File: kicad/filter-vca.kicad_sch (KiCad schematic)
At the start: 55 parts, among them J37 Conn_01x03_Male, U10 TL074, U12 LM13700, U13 LM13700, U15 TL072

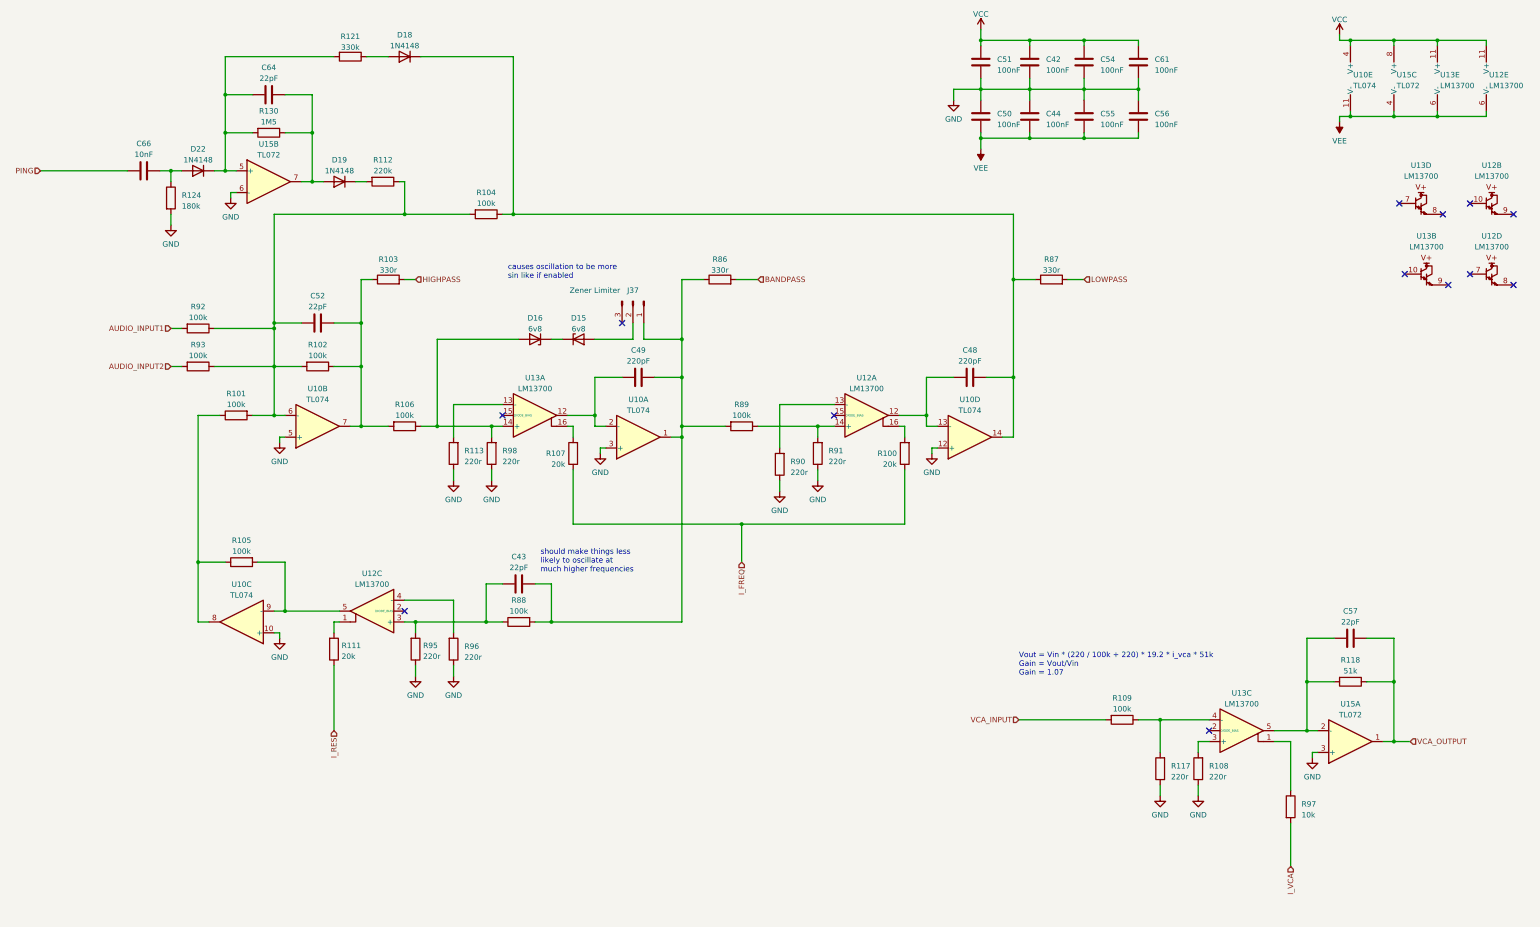
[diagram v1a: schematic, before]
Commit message: Updating board for new footprint libraries
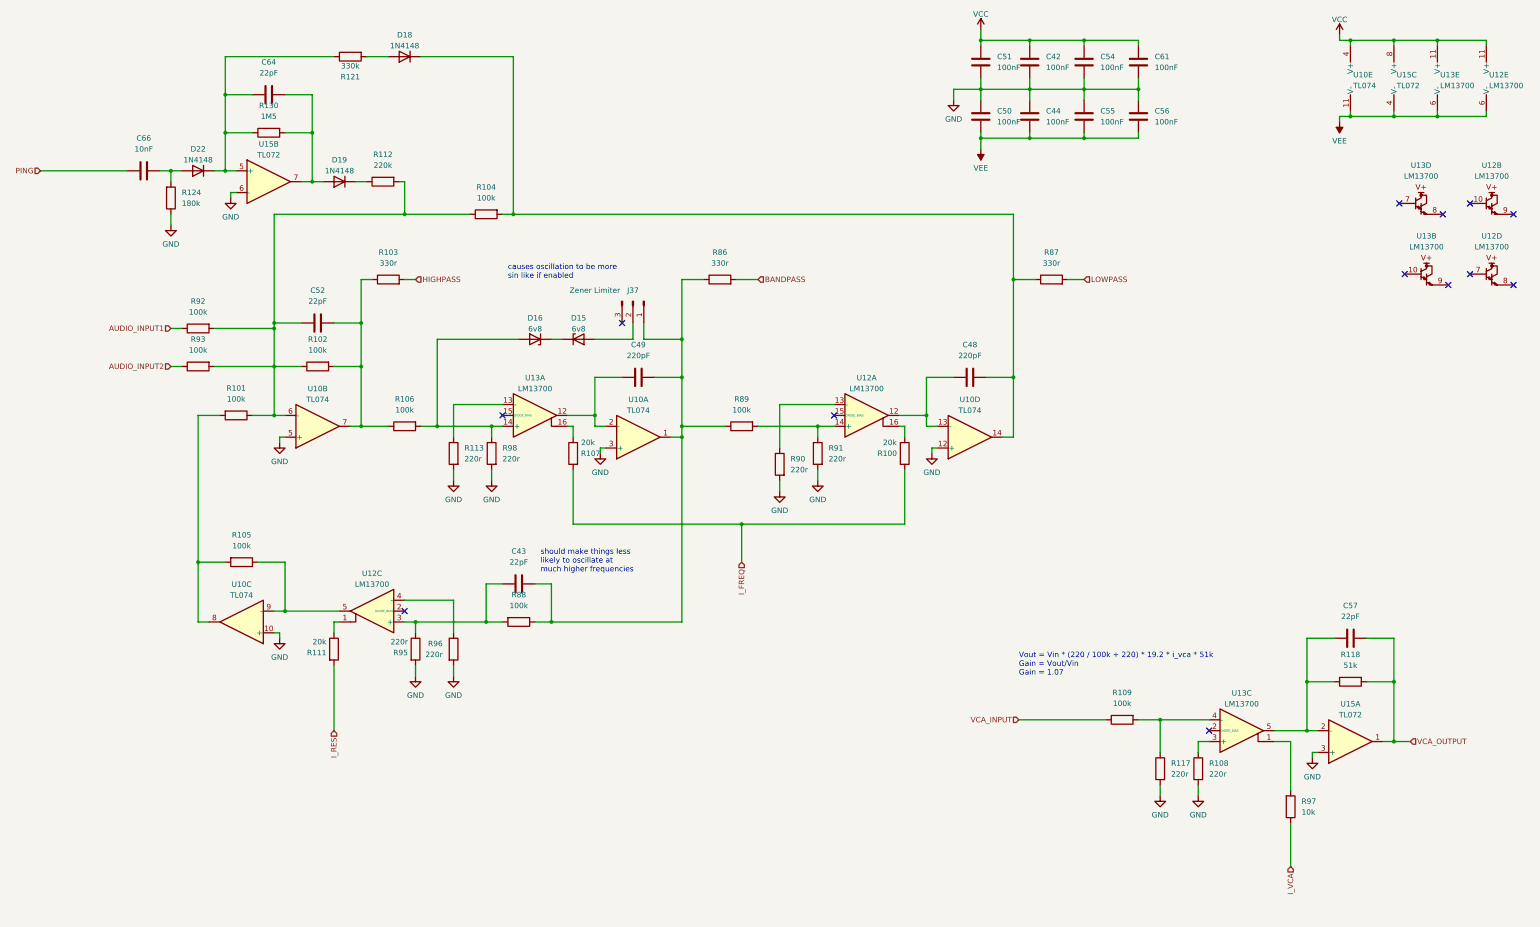
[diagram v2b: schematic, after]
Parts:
- C42, C43, C44, C48, C49, C50, C51, C52, C54, C55, C56, C57, C61, C64, C66: symbol Rumblesan Standard Parts:C -> Rumblesan_Standard_Parts:C
- R100, R101, R102, R104, R105, R106, R107, R108, R109, R111, R112, R113, R117, R118, R121, R124, R130, R88, R89, R90, R91, R92, R93, R95, R96, R97, R98: symbol Rumblesan Standard Parts:R -> Rumblesan_Standard_Parts:R
- U10: footprint Rumblesan_Standard_Parts:DIP-14_W7.62mm_Socket -> Package_DIP:DIP-14_W7.62mm_Socket
- U12, U13: footprint Rumblesan_Standard_Parts:DIP-16_W7.62mm_Socket -> Package_DIP:DIP-16_W7.62mm_Socket
- U15: footprint Rumblesan_Standard_Parts:DIP-8_W7.62mm_Socket -> Package_DIP:DIP-8_W7.62mm_Socket
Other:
- moved on the sheet: R101, R102, R104, R105, R106, R107, R108, R109, R112, R113, R117, R118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

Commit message: Updating with rev03 changes
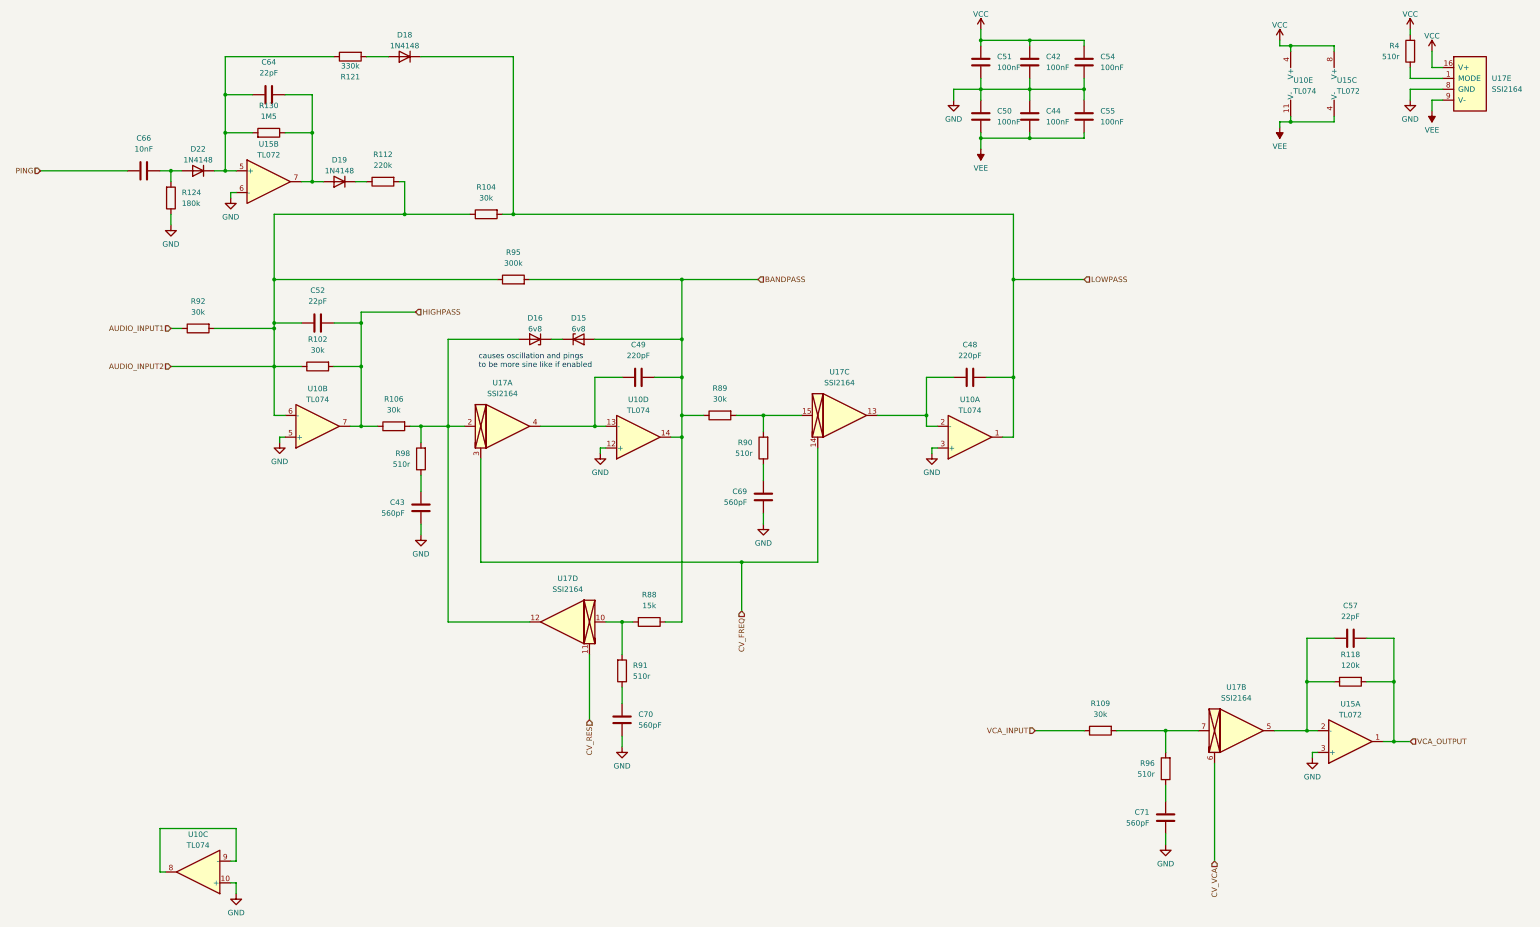
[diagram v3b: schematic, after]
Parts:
- removed C56, C61: 100nF, Rumblesan_Standard_Parts:C_Rect_L7.0mm_W2.5mm_P5.00mm, symbol Rumblesan_Standard_Parts:C
- removed J37: Conn_01x03_Male, Connector_PinHeader_2.54mm:PinHeader_1x03_P2.54mm_Vertical, symbol Connector:Conn_01x03_Pin
- removed R100, R107, R111: 20k, Rumblesan_Standard_Parts:R_Axial_DIN0207_L6.3mm_D2.5mm_P10.16mm_Horizontal, symbol Rumblesan_Standard_Parts:R
- removed R101, R105, R93: 100k, Rumblesan_Standard_Parts:R_Axial_DIN0207_L6.3mm_D2.5mm_P10.16mm_Horizontal, symbol Rumblesan_Standard_Parts:R
- removed R103, R86, R87: 330r, Rumblesan_Standard_Parts:R_Axial_DIN0207_L6.3mm_D2.5mm_P10.16mm_Horizontal, symbol Device:R
- removed R108, R113, R117, R95: 220r, Rumblesan_Standard_Parts:R_Axial_DIN0207_L6.3mm_D2.5mm_P10.16mm_Horizontal, symbol Rumblesan_Standard_Parts:R
- removed R97: 10k, Rumblesan_Standard_Parts:R_Axial_DIN0207_L6.3mm_D2.5mm_P10.16mm_Horizontal, symbol Rumblesan_Standard_Parts:R
- removed U12, U13: LM13700, Package_DIP:DIP-16_W7.62mm_Socket, symbol Amplifier_Operational:LM13700
- added C69, C70, C71: 560pF, Rumblesan_Standard_Parts:C_Rect_L7.0mm_W2.5mm_P5.00mm, symbol Rumblesan_Standard_Parts:C
- added R4: 510r, Rumblesan_Standard_Parts:R_Axial_DIN0207_L6.3mm_D2.5mm_P10.16mm_Horizontal, symbol Rumblesan_Standard_Parts:R
- added R95: 300k, Rumblesan_Standard_Parts:R_Axial_DIN0207_L6.3mm_D2.5mm_P10.16mm_Horizontal, symbol Device:R
- added U17: SSI2164, Package_DIP:DIP-16_W7.62mm_Socket, symbol Rumblesan_Audio_Chips:SSI2164
- C43: value 22pF -> 560pF
- C48, C49: footprint Rumblesan_Standard_Parts:C_Rect_L7.0mm_W2.5mm_P5.00mm -> Capacitor_THT:C_Rect_L7.0mm_W4.5mm_P5.00mm
- R102, R104, R106, R109, R89, R92: value 100k -> 30k
- R118: value 51k -> 120k
- R88: value 100k -> 15k
- R90, R91, R96, R98: value 220r -> 510r
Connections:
- net AUDIO_INPUT2: now also C52.1, R102.2, R104.2, R112.1, R92.1, U10.6 (-), R95.1
- net BANDPASS: now also C49.2, D15.2 (A), R88.2, R89.2, U10.14, R95.2
- net GND: now also C43.2, C44.2, C50.2, C69.2, C70.2, C71.2, U17.8 (GND); no longer C44.1, C50.1, R90.1, R91.1, R96.1, R98.1
- net HIGHPASS: now also C52.2, R102.1, R106.2, U10.7
- net LOWPASS: now also C48.2, D18.1 (K), R104.1, U10.1
- net VCC: now also R4.1, U17.16 (V+)
- net VEE: now also C44.1, C50.1, U17.9 (V-); no longer C44.2, C50.2
- net at C57.1, R118.2, U15.2 (-): now also U17.5
- net at U10.8: now also U10.9 (-)
- net at D16.2 (A), R106.1: now also R98.1, U17.12, U17.2; no longer R98.2
- net at C49.1: now also U10.13 (-), U17.4; no longer U10.2 (-)
- net at C64.1, D22.1 (K), R121.2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: now also R130.1; no longer R130.2
- net at R109.1: now also R96.1, U17.7
- net at C43.1: now also R98.2; no longer R88.1
- net at C64.2, D19.2 (A), U15.7: now also R130.2; no longer R130.1
- net at C48.1: now also U10.2 (-), U17.13; no longer U10.13 (-)
- net at R91.2: now also C70.1; no longer R89.1
- net at R90.2: now also C69.1
- net at R96.2: now also C71.1
- new net: R88.1, R91.1, U17.10
- new net: R4.2, U17.1 (MODE)
- new net: R89.1, R90.1, U17.15
- new net CV_FREQ: U17.14, U17.3
- new net CV_RES: U17.11
- new net CV_VCA: U17.6
- no-connect marks 13 -> 0
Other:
- note added: "causes oscillation and pings to be more sine like if enabled"
- note removed: "Vout = Vin * (220 / 100k + 220) * 19.2 * i_vca * 51k Gain = Vout/Vin Gain = 1.07"
- note removed: "causes oscillation to be more sin like if enabled"
- note removed: "should make things less likely to oscillate at much higher frequencies"
- moved on the sheet: C44, C50, R106, R109, R130, R88, R89, U10A, U10C, U10D, U10E, U15C

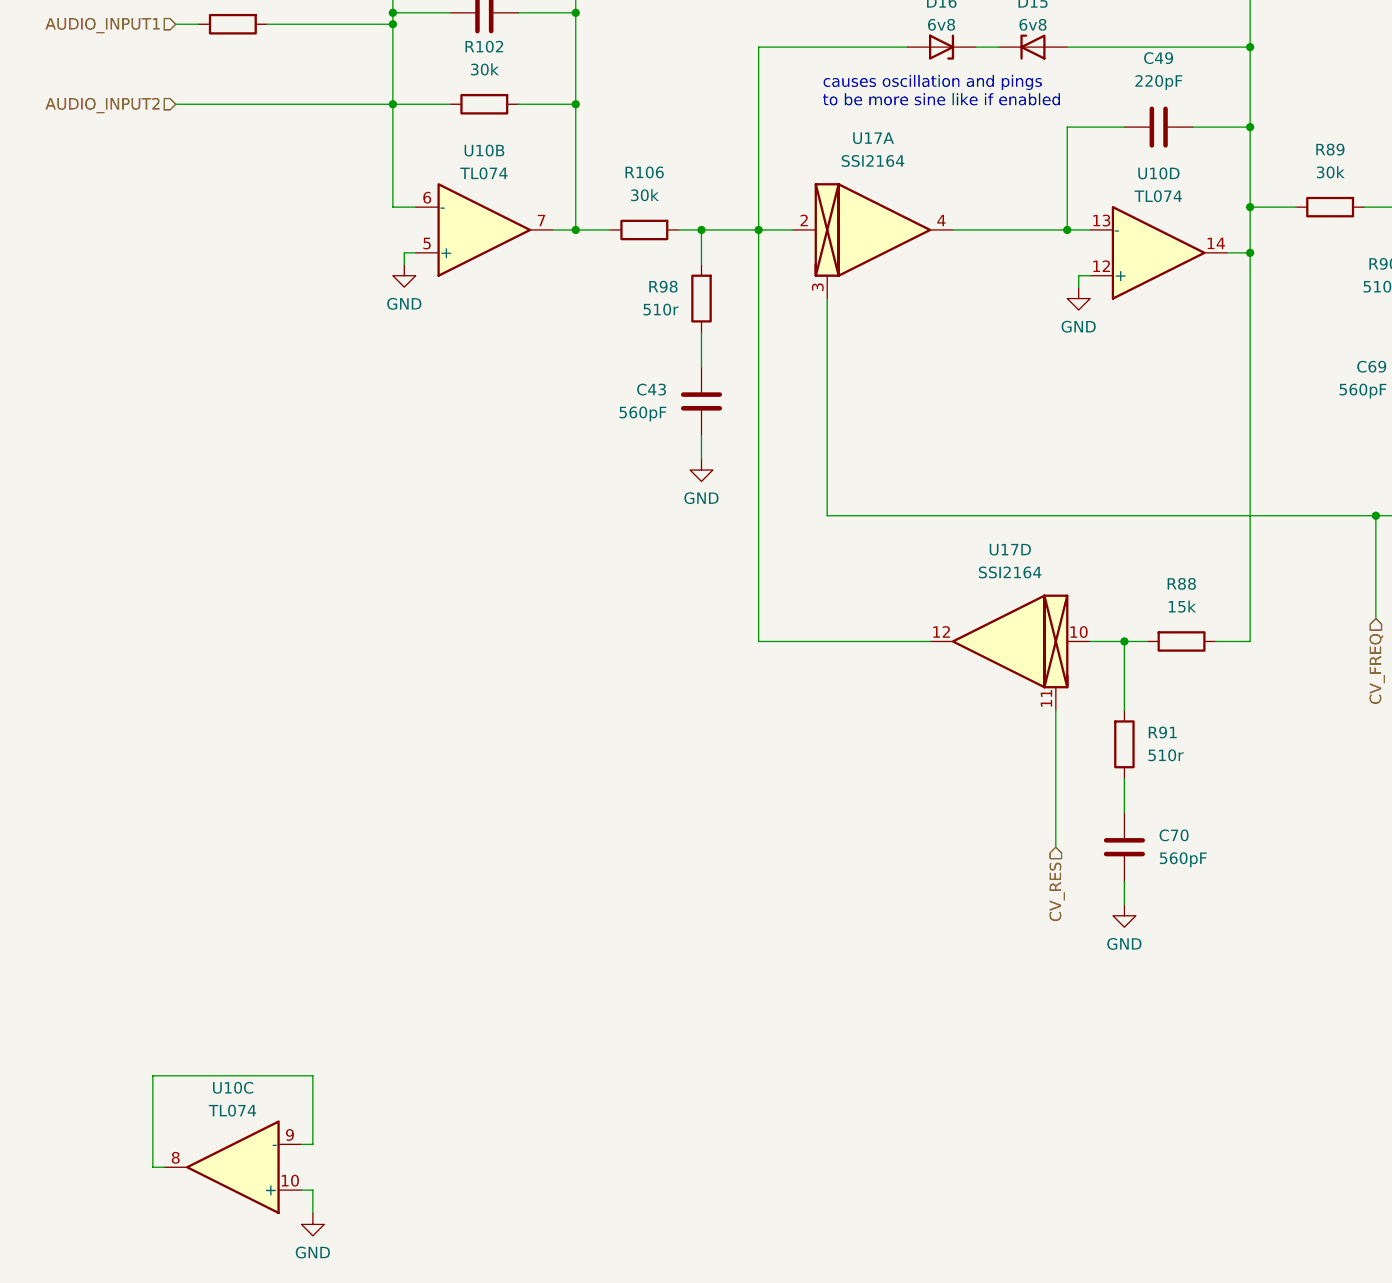
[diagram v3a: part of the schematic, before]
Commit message: Switching some opamps
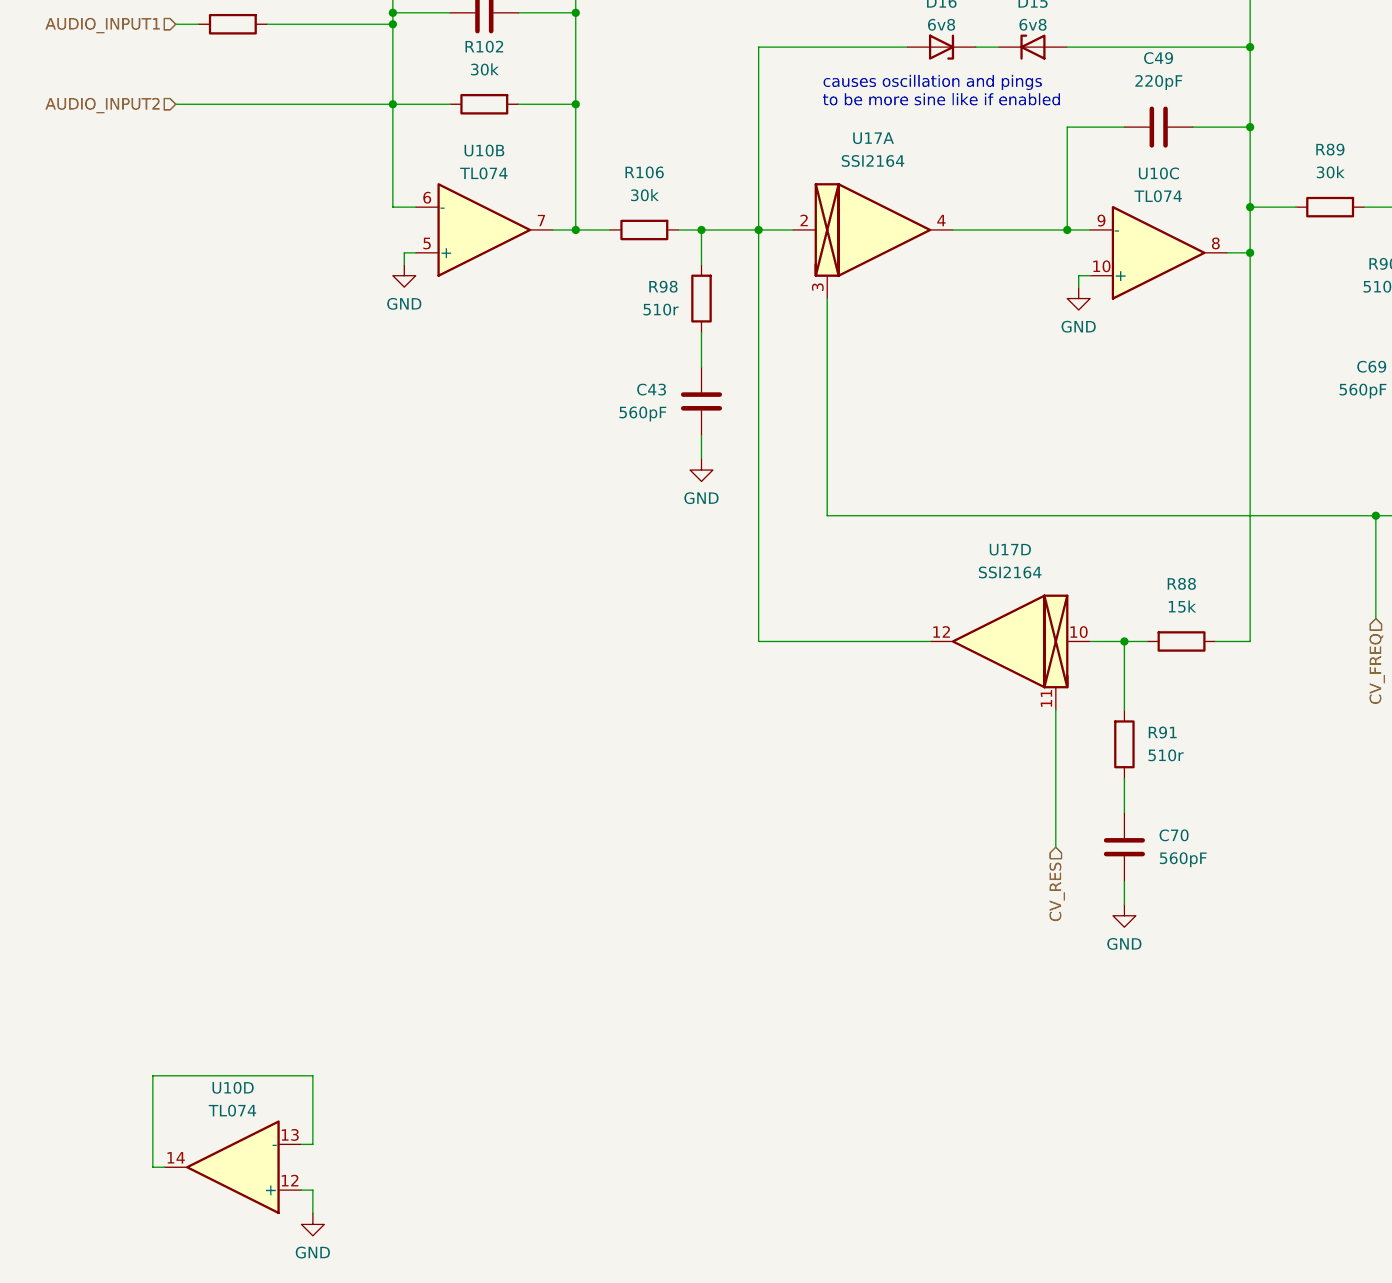
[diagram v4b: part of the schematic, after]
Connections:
- net BANDPASS: now also U10.8; no longer U10.14
- net at C49.1, U17.4: now also U10.9 (-); no longer U10.13 (-)
- new net: U10.13 (-), U10.14
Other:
- moved on the sheet: U10C, U10D
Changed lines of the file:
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@@
 	(symbol
 		(lib_id "Amplifier_Operational:TL074")
-		(at 90.17 219.71 180)
+		(at 193.04 118.11 0)
+		(mirror x)
 		(unit 3)
 		(exclude_from_sim no)
@@
 		(fields_autoplaced yes)
 		(property "Reference" "U10"
-			(at 90.17 210.9302 0)
+			(at 193.04 109.3302 0)
 			(effects
 				(font
@@
 		)
 		(property "Value" "TL074"
-			(at 90.17 213.4671 0)
+			(at 193.04 111.8671 0)
 			(effects
 				(font
@@
 		)
 		(property "Footprint" "Package_DIP:DIP-14_W7.62mm_Socket"
-			(at 91.44 222.25 0)
+			(at 191.77 120.65 0)
 			(effects
 				(font
@@
 		)
 		(property "Datasheet" "http://www.ti.com/lit/ds/symlink/tl071.pdf"
-			(at 88.9 224.79 0)
+			(at 194.31 123.19 0)
 			(effects
 				(font
@@
 		)
 		(property "Description" ""
-			(at 90.17 219.71 0)
+			(at 193.04 118.11 0)
 			(effects
 				(font
@@
 	(symbol
 		(lib_id "Amplifier_Operational:TL074")
-		(at 193.04 118.11 0)
-		(mirror x)
+		(at 90.17 219.71 180)
 		(unit 4)
 		(exclude_from_sim no)
@@
 		(fields_autoplaced yes)
 		(property "Reference" "U10"
-			(at 193.04 109.3302 0)
+			(at 90.17 210.9302 0)
 			(effects
 				(font
@@
 		)
 		(property "Value" "TL074"
-			(at 193.04 111.8671 0)
+			(at 90.17 213.4671 0)
 			(effects
 				(font
@@
 		)
 		(property "Footprint" "Package_DIP:DIP-14_W7.62mm_Socket"
-			(at 191.77 120.65 0)
+			(at 91.44 222.25 0)
 			(effects
 				(font
@@
 		)
 		(property "Datasheet" "http://www.ti.com/lit/ds/symlink/tl071.pdf"
-			(at 194.31 123.19 0)
+			(at 88.9 224.79 0)
 			(effects
 				(font
@@
 		)
 		(property "Description" ""
-			(at 193.04 118.11 0)
-			(effects
-				(font
+			(at 90.17 219.71 0)
+			(effects
+				(font
